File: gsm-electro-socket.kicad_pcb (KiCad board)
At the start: 2 copper layers, 3 parts, among them U1 ArduinoProMini

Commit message: update footprints
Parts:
- removed R1: R_Small, Resistors_SMD:R_1210
- removed R2: R_Small, Resistors_SMD:R_0402
- added R1_100: R_Small, Resistors_SMD:R_0402, F.Cu at (146.7, 101.6)
- added R2_370: R_Small, Resistors_SMD:R_0402, F.Cu at (143.5, 101.6)
- added U2: SIM800C, boards:sim800c, F.Cu at (142.3, 84.9)
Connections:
- U1 pad 1: (no net) -> Net-(R1_100-Pad1)
- U1 pad 17: Net-(R2-Pad2) -> (no net)
- U1 pad 2: (no net) -> Net-(U1-Pad2)
- U1 pad 23: Net-(R1-Pad2) -> (no net)
- U1 pad 25: (no net) -> +5V
- U1 pad 27: (no net) -> GND
- U1 pad 28: Net-(R1-Pad1) -> (no net)
- U1 pad 30: (no net) -> GND
- U1 pad 4: (no net) -> GND
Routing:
- net +5V: track 0.00 -> 65.9 mm
- net GND: track 0.00 -> 54.7 mm
- net Net-(R1-Pad2): track 19.7 -> 0.00 mm
- net Net-(R2-Pad2): track 18.5 -> 0.00 mm
- net Net-(R1_100-Pad2): track 0.00 -> 12.3 mm
- net Net-(U1-Pad2): track 0.00 -> 7.07 mm
- net Net-(R1_100-Pad1): track 0.00 -> 2.43 mm
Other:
- net class Default: trace_width 0.25 -> 0.8

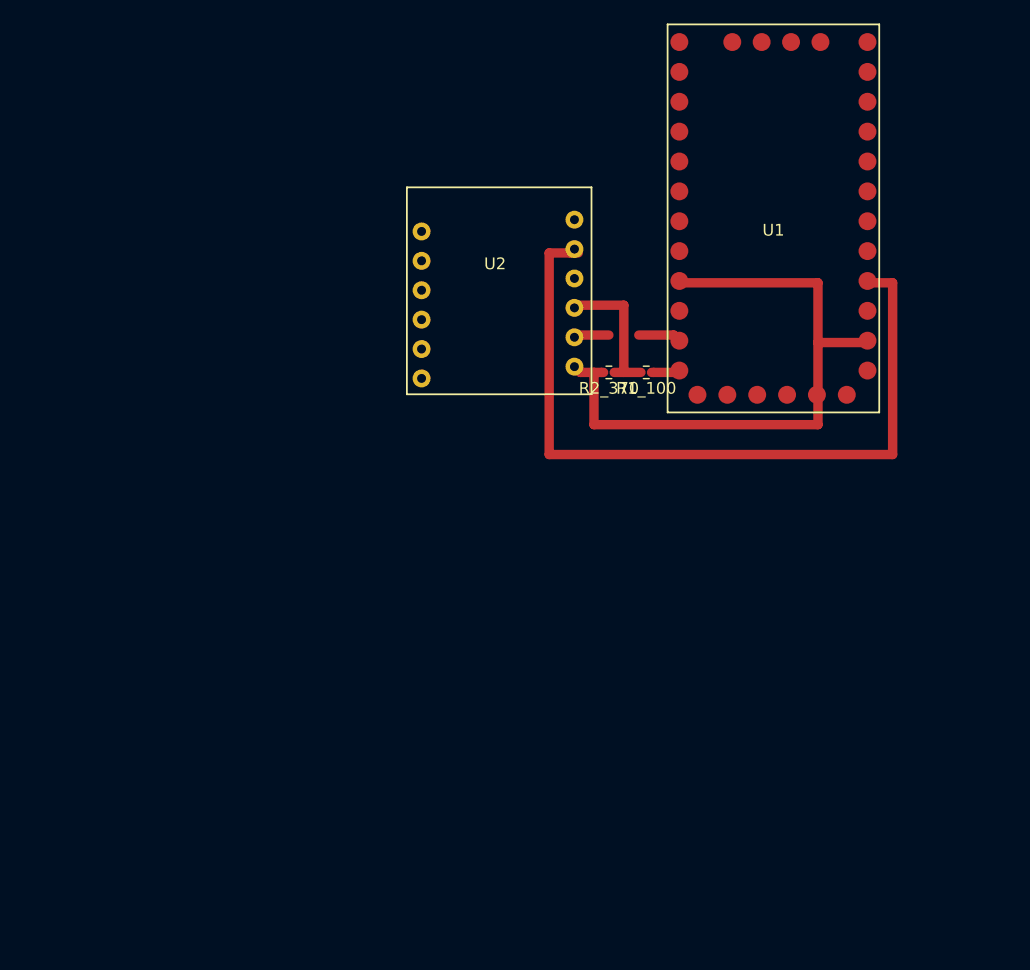
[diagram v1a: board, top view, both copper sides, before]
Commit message: change arduino to atmega328p
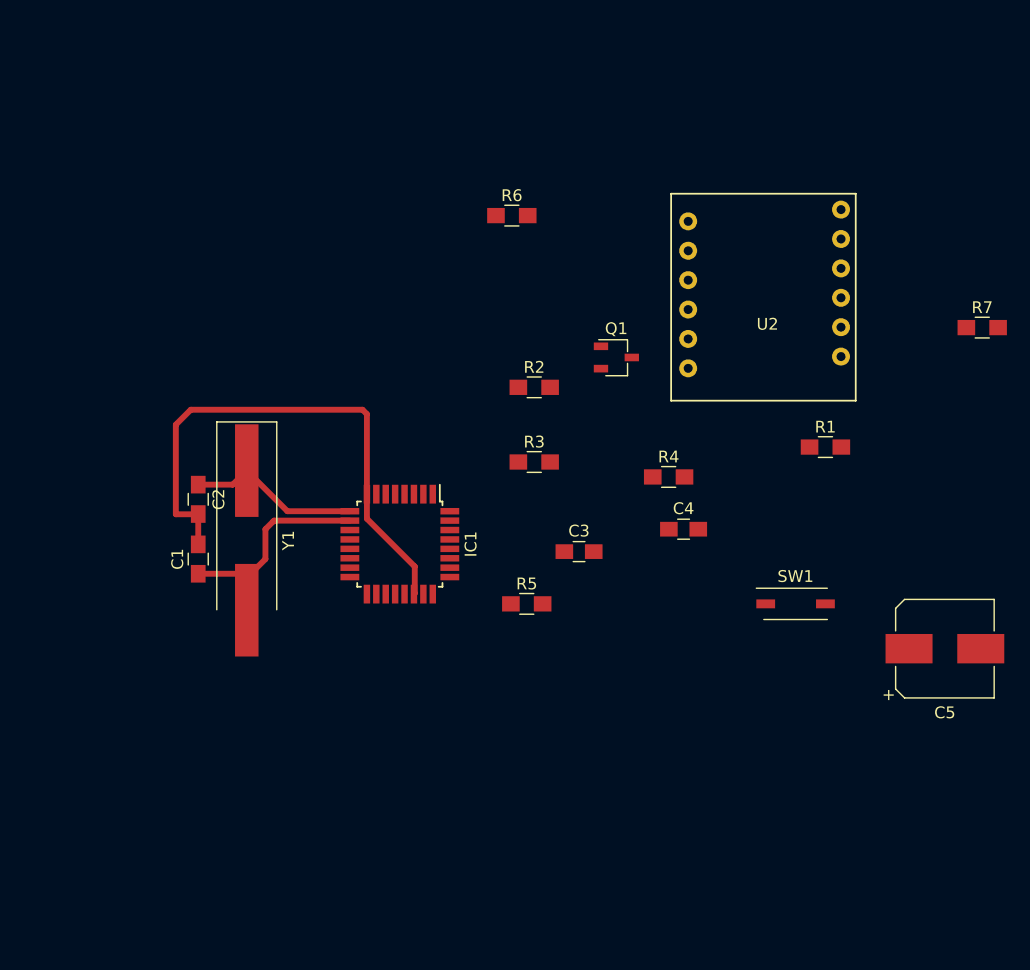
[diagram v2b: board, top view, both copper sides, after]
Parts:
- removed R1_100, R2_370: R_Small, Resistors_SMD:R_0402
- removed U1: ArduinoProMini, boards:ArduinoProMini
- added C1: 22pF, Capacitors_SMD:C_0805_HandSoldering, F.Cu at (108.6, 117.5)
- added C2: 22pF, Capacitors_SMD:C_0805_HandSoldering, F.Cu at (108.6, 112.4)
- added C3: 0,1mF, Capacitors_SMD:C_0805_HandSoldering, F.Cu at (141.0, 116.8)
- added C4: 0,1mF, Capacitors_SMD:C_0805_HandSoldering, F.Cu at (149.9, 114.9)
- added C5: 47mF, Capacitors_SMD:CP_Elec_8x10.5, F.Cu at (172.1, 125.1)
- added IC1: ATMEGA328-P, Housings_QFP:TQFP-32_7x7mm_Pitch0.8mm, F.Cu at (125.7, 116.2)
- added Q1: BC337, TO_SOT_Packages_SMD:TSOT-23, F.Cu at (144.1, 100.3)
- added R1: 1k, Resistors_SMD:R_0805_HandSoldering, F.Cu at (161.9, 108.0)
- added R2: 10k, Resistors_SMD:R_0805_HandSoldering, F.Cu at (137.2, 102.9)
- added R3: 100k, Resistors_SMD:R_0805_HandSoldering, F.Cu at (137.2, 109.2)
- added R4: 47k, Resistors_SMD:R_0805_HandSoldering, F.Cu at (148.6, 110.5)
- added R5: 4.7k, Resistors_SMD:R_0805_HandSoldering, F.Cu at (136.5, 121.3)
- added R6: 370, Resistors_SMD:R_0805_HandSoldering, F.Cu at (135.3, 88.3)
- added R7: 100, Resistors_SMD:R_0805_HandSoldering, F.Cu at (175.3, 97.8)
- added SW1: RESET, Buttons_Switches_SMD:SW_DIP_x1_W5.08mm_Slide_Copal_CHS-A, F.Cu at (159.4, 121.3)
- added Y1: 16Mhz, Crystals:Crystal_SMD_HC49-SD_HandSoldering, F.Cu at (112.7, 115.9)
- moved U2 21.1 mm to (148.5, 105.0), turned to 0 degrees
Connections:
- U2 pad 10: (no net) -> Net-(R1-Pad2)
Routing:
- net +5V: track 65.9 -> 0.00 mm
- net Net-(C1-Pad1): track 0.00 -> 16.3 mm
- net Net-(C2-Pad1): track 0.00 -> 14.8 mm
- net Net-(R6-Pad1): track 12.3 -> 0.00 mm
- net GND: track 54.7 -> 46.1 mm
- net Net-(IC1-Pad2): track 7.07 -> 0.00 mm
- net Net-(R1_100-Pad1): track 2.43 -> 0.00 mm
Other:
- net class Default: trace_width 0.8 -> 0.5

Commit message: added same tracks
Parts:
- moved R1 59.2 mm to (116.7, 146.3)
- moved Q1 55.6 mm to (111.2, 145.1), turned to 270 degrees
- moved R4 53.9 mm to (107.3, 145.1), turned to 90 degrees
- moved R7 51.3 mm to (124.0, 98.1), turned to 90 degrees
- moved C5 41.3 mm to (131.5, 133.0)
- moved R3 39.7 mm to (122.8, 146.2), turned to 180 degrees
- moved R5 34.2 mm to (107.3, 139.0), turned to 270 degrees
- moved SW1 23.6 mm to (136.9, 114.1), turned to 90 degrees
- moved R6 14.2 mm to (122.2, 94.0), turned to 180 degrees
- moved C3 14.1 mm to (129.6, 125.2), turned to 180 degrees
- moved C4 12.3 mm to (140.2, 122.6)
- moved R2 12.1 mm to (143.2, 113.4), turned to 90 degrees
- moved C1 9.45 mm to (99.1, 117.9)
- moved C2 9.45 mm to (99.1, 112.8)
- moved U2 2.92 mm to (150.6, 103.0), turned to 90 degrees
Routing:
- net Net-(R1-Pad2): track 0.00 -> 98.2 mm
- net +5V: track 0.00 -> 95.5 mm
- net GND: track 46.1 -> 110.2 mm
- net Net-(IC1-Pad14): track 0.00 -> 35.7 mm
- net Net-(R6-Pad1): track 0.00 -> 22.8 mm
- net RST: track 0.00 -> 18.4 mm
- net Net-(IC1-Pad2): track 0.00 -> 18.2 mm
- net Net-(IC1-Pad3): track 0.00 -> 14.2 mm
- net Net-(C1-Pad1): track 16.3 -> 26.3 mm
- net Net-(C2-Pad1): track 14.8 -> 24.3 mm
- net Net-(Q1-Pad2): track 0.00 -> 6.43 mm
- net Net-(C3-Pad2): track 0.00 -> 5.76 mm
- net Net-(Q1-Pad1): track 0.00 -> 5.73 mm
- net Net-(Q1-Pad3): track 0.00 -> 3.88 mm
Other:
- net class bold track added: clearance 0.2, trace_width 1, via_dia 0.6, via_drill 0.4

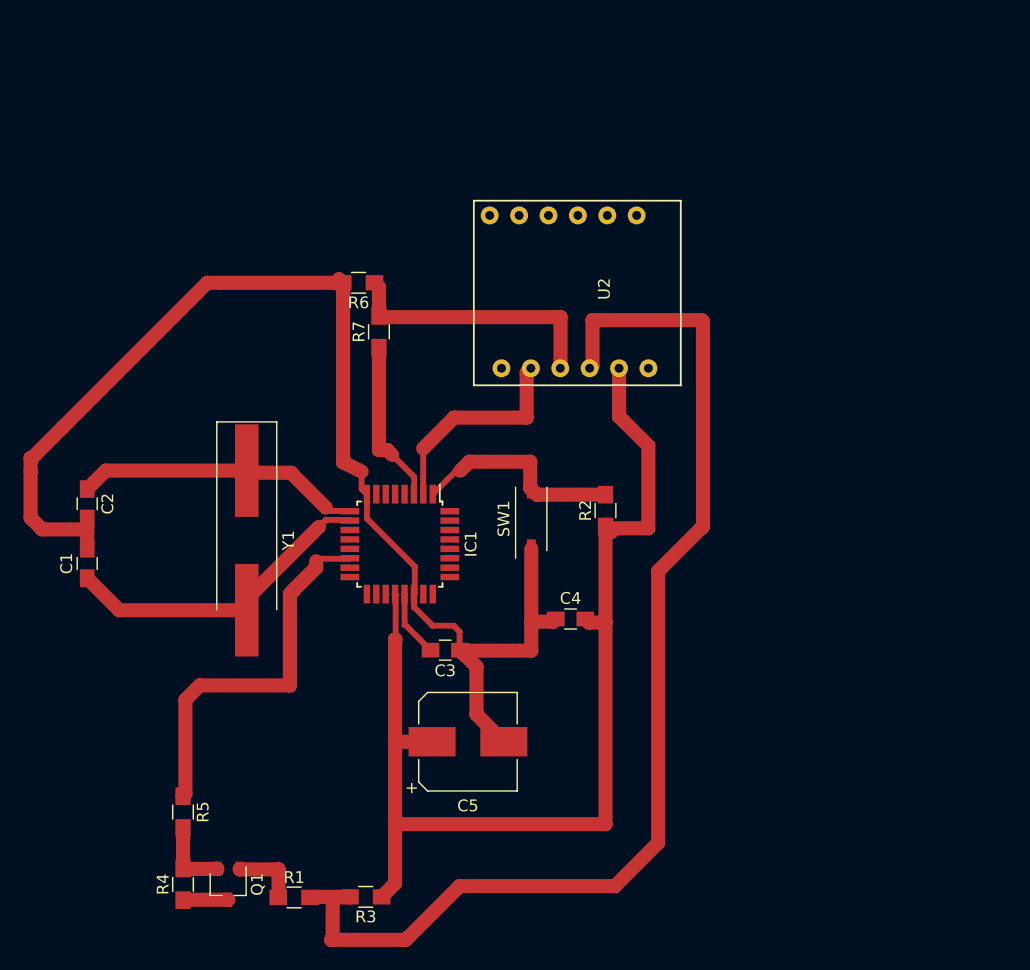
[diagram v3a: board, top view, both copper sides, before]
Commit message: added power converter(step-down)
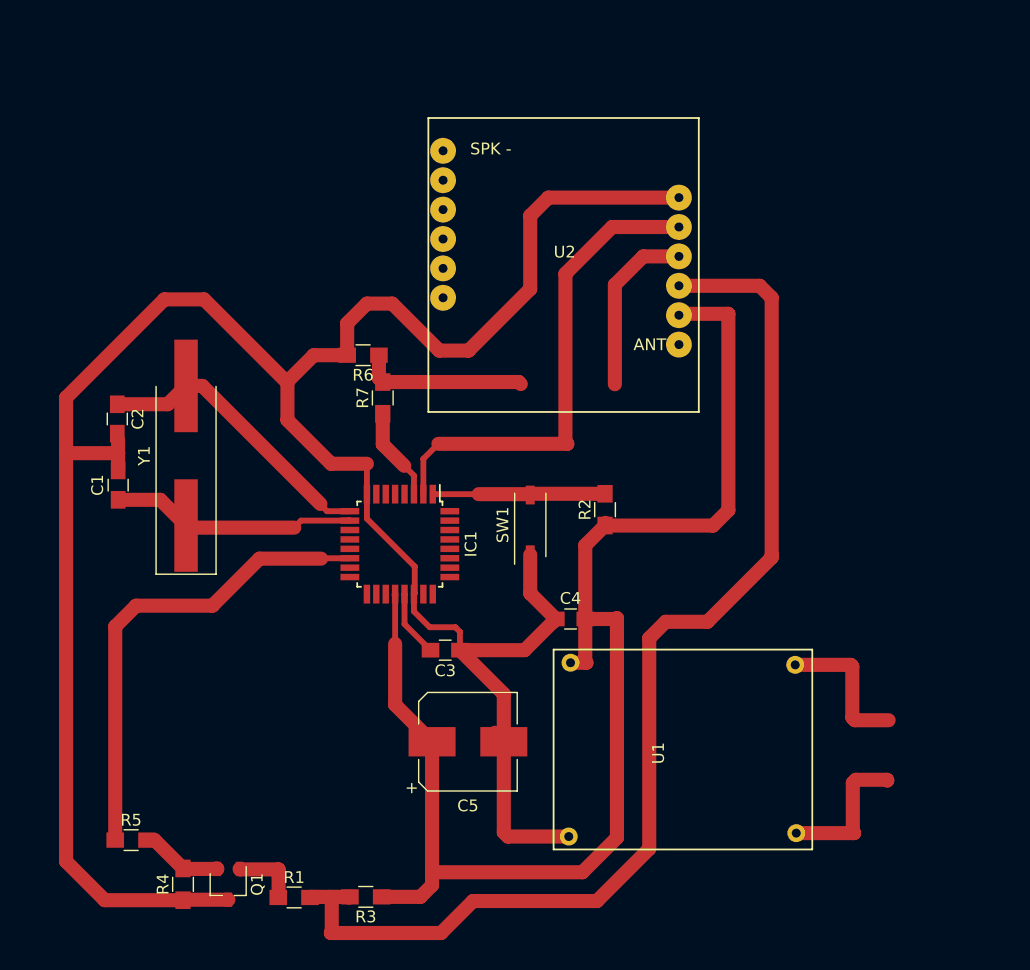
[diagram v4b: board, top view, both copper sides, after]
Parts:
- added U1: PWRCONV, boards:PwrConvStepDown, F.Cu at (138.8, 125.2)
- R6: value 370 -> 150
- moved U2 23.0 mm to (151.2, 80.0), turned to 180 degrees
- moved Y1 8.86 mm to (107.5, 108.7), turned to 90 degrees
- moved C2 7.65 mm to (101.7, 105.6)
- moved C1 7.17 mm to (101.8, 111.2)
- moved R6 6.17 mm to (122.6, 100.1)
- moved R7 5.63 mm to (124.3, 103.8)
- moved R5 5.02 mm to (102.9, 141.4), turned to 0 degrees
- moved SW1 0.52 mm to (136.8, 114.6)
- moved R2 0.09 mm to (143.2, 113.3)
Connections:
- net RST renamed Net-(IC1-Pad1)
- IC1 pad 11: (no net) -> Net-(IC1-Pad11)
- IC1 pad 12: (no net) -> Net-(IC1-Pad12)
- IC1 pad 13: (no net) -> Net-(IC1-Pad13)
- IC1 pad 15: (no net) -> Net-(IC1-Pad15)
- IC1 pad 16: (no net) -> Net-(IC1-Pad16)
- IC1 pad 17: (no net) -> Net-(IC1-Pad17)
- IC1 pad 18: (no net) -> Net-(IC1-Pad18)
- IC1 pad 19: (no net) -> Net-(IC1-Pad19)
- IC1 pad 23: (no net) -> Net-(IC1-Pad23)
- IC1 pad 24: (no net) -> Net-(IC1-Pad24)
- IC1 pad 25: (no net) -> Net-(IC1-Pad25)
- IC1 pad 26: (no net) -> Net-(IC1-Pad26)
- IC1 pad 27: (no net) -> Net-(IC1-Pad27)
- IC1 pad 28: (no net) -> Net-(IC1-Pad28)
- IC1 pad 4: (no net) -> Net-(IC1-Pad4)
- IC1 pad 5: (no net) -> Net-(IC1-Pad5)
- IC1 pad 6: (no net) -> Net-(IC1-Pad6)
- Q1 pad 3: Net-(Q1-Pad3) -> GND
- R4 pad 1: Net-(Q1-Pad3) -> GND
- U2 pad 1: (no net) -> Net-(U2-Pad1)
- U2 pad 12: (no net) -> Net-(U2-Pad12)
- U2 pad 2: (no net) -> Net-(U2-Pad2)
- U2 pad 3: (no net) -> Net-(U2-Pad3)
- U2 pad 4: (no net) -> Net-(U2-Pad4)
- U2 pad 5: (no net) -> Net-(U2-Pad5)
- U2 pad 6: (no net) -> Net-(U2-Pad6)
- Y1 pad 1: Net-(C2-Pad1) -> Net-(C1-Pad1)
- Y1 pad 2: Net-(C1-Pad1) -> Net-(C2-Pad1)
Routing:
- net GND: track 110.2 -> 220.0 mm
- net Net-(IC1-Pad2): track 18.2 -> 41.6 mm
- net +5V: track 95.5 -> 115.3 mm
- net +12V: track 0.00 -> 12.4 mm
- net Net-(R6-Pad1): track 22.8 -> 29.1 mm
- net Net-(IC1-Pad3): track 14.2 -> 7.96 mm
- net Net-(C1-Pad1): track 26.3 -> 21.0 mm
- net Net-(IC1-Pad14): track 35.7 -> 40.5 mm
- net Net-(Q1-Pad3): track 3.88 -> 0.00 mm
- net Net-(IC1-Pad1): track 18.4 -> 15.3 mm
- net Net-(Q1-Pad2): track 6.43 -> 7.05 mm

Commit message: update schema
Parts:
- removed SW1: RESET, Buttons_Switches_SMD:SW_DIP_x1_W5.08mm_Slide_Copal_CHS-A
- added D1: LED, LEDs:LED_D2.0mm_W4.0mm_H2.8mm_FlatTop, F.Cu at (136.0, 118.0)
- added P1: CONN_01X03, Pin_Headers:Pin_Header_Angled_1x03_Pitch2.54mm, F.Cu at (142.6, 118.6)
- added P2: CONN_01X03, Pin_Headers:Pin_Header_Angled_1x03_Pitch2.54mm, F.Cu at (111.9, 128.5)
- added R8: 1k, Resistors_SMD:R_0805_HandSoldering, F.Cu at (137.7, 118.0)
- moved R2 6.84 mm to (150.0, 112.8)
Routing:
- net Net-(IC1-Pad19): track 0.00 -> 21.5 mm
- net Net-(IC1-Pad18): track 0.00 -> 17.2 mm
- net Net-(IC1-Pad17): track 0.00 -> 15.7 mm
- net Net-(IC1-Pad1): track 15.3 -> 28.4 mm
- net Net-(D1-Pad2): track 0.00 -> 3.90 mm
- net +5V: track 115.3 -> 118.1 mm
- net GND: track 220.0 -> 222.2 mm

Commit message: update pcb
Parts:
- IC1: value ATMEGA328-P -> ATMEGA328P-A
- moved U2 41.6 mm to (160.3, 120.5)
- moved R8 31.3 mm to (106.9, 112.2), turned to 180 degrees
- moved U1 27.0 mm to (112.5, 119.0), turned to 180 degrees
- moved R2 26.8 mm to (131.5, 132.2)
- moved P1 26.0 mm to (119.5, 130.6), turned to 90 degrees
- moved R5 25.7 mm to (109.8, 116.6), turned to 180 degrees
- moved D1 24.6 mm to (112.1, 112.2), turned to 0 degrees
- moved R4 21.8 mm to (103.1, 123.8), turned to 0 degrees
- moved C4 20.2 mm to (120.7, 127.7), turned to 180 degrees
- moved R3 20.1 mm to (106.4, 134.6)
- moved R1 19.7 mm to (102.0, 133.2), turned to 270 degrees
- moved Q1 19.3 mm to (103.1, 127.6), turned to 180 degrees
- moved C5 18.7 mm to (150.0, 130.4), turned to 90 degrees
- moved C2 16.6 mm to (118.1, 103.1), turned to 180 degrees
- moved C1 13.3 mm to (112.4, 103.1), turned to 0 degrees
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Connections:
- IC1 pad 10: Net-(C1-Pad1) -> Net-(IC1-Pad10)
- IC1 pad 12: Net-(IC1-Pad12) -> Net-(D1-Pad2)
- IC1 pad 18: Net-(IC1-Pad18) -> +5V
- IC1 pad 20: +5V -> Net-(C3-Pad2)
- IC1 pad 21: Net-(C3-Pad2) -> GND
- IC1 pad 22: GND -> Net-(IC1-Pad22)
- IC1 pad 25: Net-(D1-Pad2) -> Net-(IC1-Pad25)
- IC1 pad 29: (no net) -> Net-(IC1-Pad29)
- IC1 pad 3: Net-(IC1-Pad3) -> GND
- IC1 pad 30: (no net) -> Net-(IC1-Pad30)
- IC1 pad 31: (no net) -> Net-(IC1-Pad31)
- IC1 pad 32: (no net) -> Net-(IC1-Pad32)
- IC1 pad 4: Net-(IC1-Pad4) -> +5V
- IC1 pad 5: Net-(IC1-Pad5) -> GND
- IC1 pad 6: Net-(IC1-Pad6) -> +5V
- IC1 pad 7: +5V -> Net-(C2-Pad1)
- IC1 pad 8: GND -> Net-(C1-Pad1)
- IC1 pad 9: Net-(C2-Pad1) -> Net-(IC1-Pad9)
- P1 pad 1: GND -> +5V
- P1 pad 2: +5V -> GND
- P1 pad 3: Net-(IC1-Pad1) -> Net-(IC1-Pad29)
- P2 pad 1: Net-(IC1-Pad17) -> Net-(IC1-Pad15)
- P2 pad 2: Net-(IC1-Pad18) -> Net-(IC1-Pad16)
- P2 pad 3: Net-(IC1-Pad19) -> Net-(IC1-Pad17)
- R2 pad 2: Net-(IC1-Pad1) -> Net-(IC1-Pad29)
- R7 pad 1: Net-(IC1-Pad3) -> Net-(IC1-Pad31)
- U2 pad 8: Net-(IC1-Pad2) -> Net-(IC1-Pad30)
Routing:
- net Net-(IC1-Pad30): track 0.00 -> 46.7 mm
- net Net-(IC1-Pad2): track 41.6 -> 0.00 mm
- net GND: track 222.2 -> 184.9 mm
- net Net-(R6-Pad1): track 29.1 -> 63.4 mm
- net Net-(IC1-Pad14): track 40.5 -> 10.8 mm
- net Net-(IC1-Pad1): track 28.4 -> 0.14 mm
- net Net-(IC1-Pad29): track 0.00 -> 26.1 mm
- net Net-(IC1-Pad19): track 21.5 -> 0.00 mm
- net Net-(R1-Pad2): track 98.3 -> 80.7 mm
- net Net-(IC1-Pad18): track 17.2 -> 0.00 mm
- net Net-(C2-Pad1): track 24.4 -> 11.2 mm
- net Net-(IC1-Pad16): track 0.00 -> 9.73 mm
- net Net-(IC1-Pad31): track 0.00 -> 9.12 mm
- net Net-(IC1-Pad3): track 7.96 -> 0.00 mm
- net Net-(IC1-Pad15): track 0.00 -> 7.93 mm
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
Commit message: update pcb
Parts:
- added P3: CONN_01X02, Pin_Headers:Pin_Header_Angled_1x02_Pitch2.54mm, F.Cu at (103.3, 144.0)
- added P4: CONN_01X03, Pin_Headers:Pin_Header_Angled_1x03_Pitch2.54mm, F.Cu at (127.0, 106.3)
- moved R6 13.8 mm to (142.3, 103.1)
- moved R7 9.59 mm to (143.7, 107.3)
- moved R2 8.11 mm to (139.6, 131.9)
- moved U2 1.73 mm to (160.2, 122.2)
- moved U1 0.28 mm to (112.5, 119.3)
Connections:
- U1 pad 1: +12V -> Net-(P3-Pad2)
- U1 pad 2: GND -> Net-(P3-Pad1)
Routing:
- net Net-(P3-Pad1): track 0.00 -> 24.9 mm
- net Net-(IC1-Pad29): track 26.1 -> 39.4 mm
- net +5V: track 121.3 -> 133.4 mm
- net Net-(R6-Pad1): track 63.4 -> 52.0 mm
- net Net-(IC1-Pad1): track 0.14 -> 8.72 mm
- net Net-(P3-Pad2): track 0.00 -> 7.88 mm
- net +12V: track 7.88 -> 0.00 mm
- net Net-(IC1-Pad31): track 9.12 -> 16.0 mm
- net Net-(R1-Pad2): track 80.7 -> 84.1 mm
- net GND: track 184.9 -> 183.3 mm
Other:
- board text added: "+12v"
- board text added: "+4,2v"
- board text added: "ANT"
- board text added: "GND"
- board text added: "MISO"
- board text added: "MOSI"
- board text added: "OUT"
- board text added: "RST"
- board text added: "SCK"
